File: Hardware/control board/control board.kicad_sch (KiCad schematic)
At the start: 11 parts, among them J1 Screw_Terminal_01x02, SW1 SW_Push

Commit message: footprint work
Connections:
- net solenoid 1/Sol port: now also A1.D23; no longer A1.D25
- net solenoid 2/Sol port: now also A1.D25; no longer A1.D26
- no-connect marks 0 -> 81

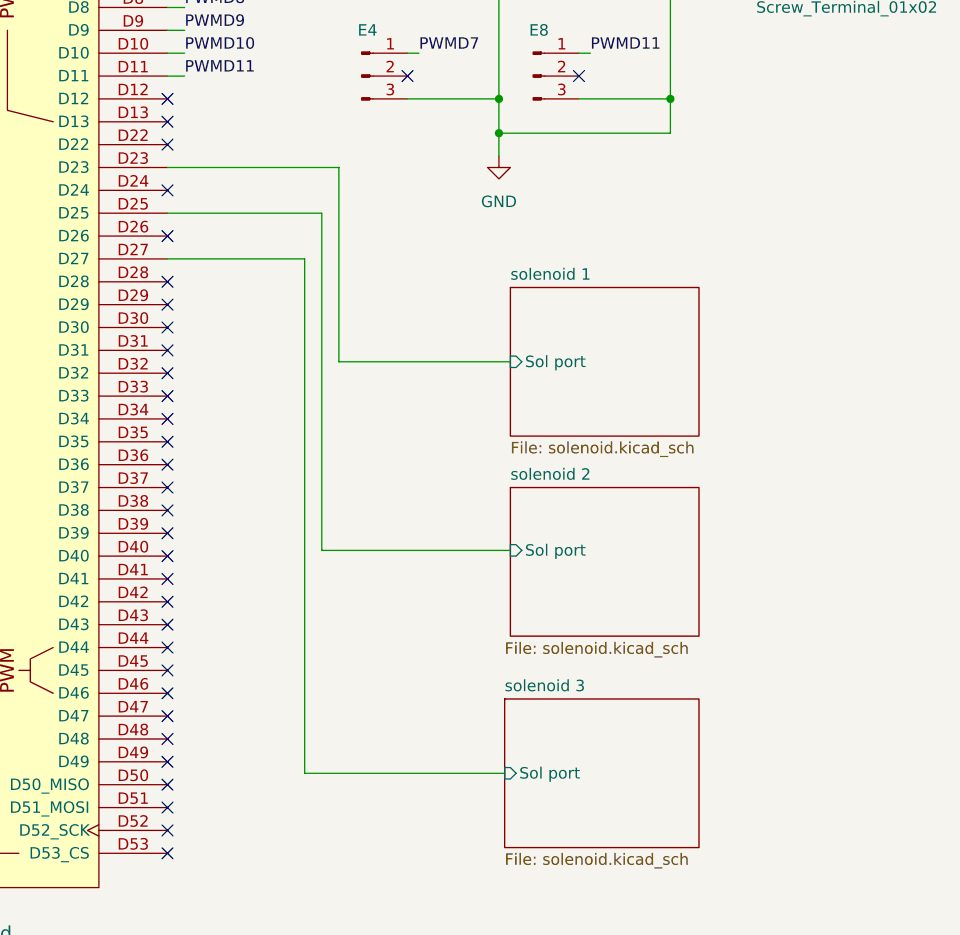
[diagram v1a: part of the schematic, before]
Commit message: laid out components prior to order
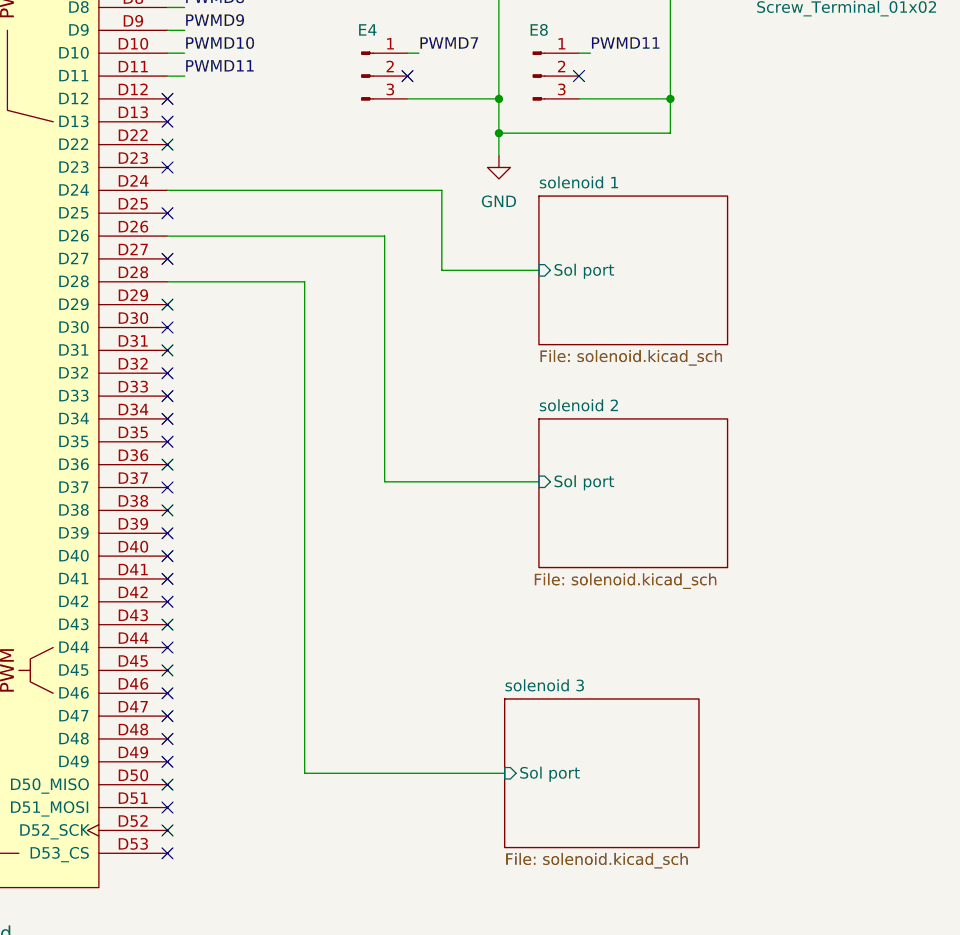
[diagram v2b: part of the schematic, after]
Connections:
- net solenoid 1/Sol port: now also A1.D24; no longer A1.D23
- net solenoid 2/Sol port: now also A1.D26; no longer A1.D25
- net solenoid 3/Sol port: now also A1.D28; no longer A1.D27
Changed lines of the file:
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@@
   (no_connect (at 93.345 129.54))
   (no_connect (at 93.345 111.76))
+  (no_connect (at 93.345 76.2))
   (no_connect (at 27.305 129.54))
   (no_connect (at 93.345 134.62))
@@
   (no_connect (at 27.305 48.26))
   (no_connect (at 27.305 40.64))
-  (no_connect (at 93.345 78.74))
   (no_connect (at 61.595 26.67))
   (no_connect (at 27.305 55.88))
@@
   (no_connect (at 93.345 96.52))
   (no_connect (at 93.345 124.46))
+  (no_connect (at 93.345 81.28))
   (no_connect (at 27.305 109.22))
   (no_connect (at 27.305 93.98))
-  (no_connect (at 93.345 83.82))
   (no_connect (at 53.975 26.67))
   (no_connect (at 27.305 134.62))
@@
   (no_connect (at 93.345 114.3))
   (no_connect (at 93.345 91.44))
+  (no_connect (at 93.345 71.12))
   (no_connect (at 27.305 96.52))
   (no_connect (at 27.305 104.14))
@@
   (no_connect (at 27.305 111.76))
   (no_connect (at 27.305 73.66))
-  (no_connect (at 93.345 73.66))
   (no_connect (at 27.305 78.74))
   (no_connect (at 93.345 139.7))
@@
   (no_connect (at 27.305 81.28))
   (no_connect (at 27.305 66.04))
+  (wire (pts (xy 134.62 82.55) (xy 123.825 82.55))
+    (stroke (width 0) (type default))
+  )
   (wire (pts (xy 139.065 50.8) (xy 149.225 50.8))
     (stroke (width 0) (type default))
   )
-  (wire (pts (xy 112.395 71.12) (xy 112.395 92.71))
-    (stroke (width 0) (type default))
-  )
   (wire (pts (xy 93.345 58.42) (xy 95.25 58.42))
     (stroke (width 0) (type default))
   )
-  (wire (pts (xy 110.49 76.2) (xy 93.345 76.2))
-    (stroke (width 0) (type default))
-  )
   (wire (pts (xy 149.225 50.8) (xy 149.225 63.5))
     (stroke (width 0) (type default))
   )
+  (wire (pts (xy 117.475 78.74) (xy 117.475 106.045))
+    (stroke (width 0) (type default))
+  )
   (wire (pts (xy 130.81 138.43) (xy 108.585 138.43))
     (stroke (width 0) (type default))
@@
     (stroke (width 0) (type default))
   )
+  (wire (pts (xy 93.345 78.74) (xy 117.475 78.74))
+    (stroke (width 0) (type default))
+  )
+  (wire (pts (xy 123.825 73.66) (xy 93.345 73.66))
+    (stroke (width 0) (type default))
+  )
   (wire (pts (xy 93.345 53.34) (xy 95.25 53.34))
     (stroke (width 0) (type default))
@@
     (stroke (width 0) (type default))
   )
-  (wire (pts (xy 131.445 113.665) (xy 110.49 113.665))
-    (stroke (width 0) (type default))
-  )
   (wire (pts (xy 23.495 137.16) (xy 23.495 139.7))
     (stroke (width 0) (type default))
@@
     (stroke (width 0) (type default))
   )
-  (wire (pts (xy 108.585 81.28) (xy 108.585 138.43))
+  (wire (pts (xy 123.825 82.55) (xy 123.825 73.66))
     (stroke (width 0) (type default))
   )
@@
     (stroke (width 0) (type default))
   )
+  (wire (pts (xy 108.585 138.43) (xy 108.585 83.82))
+    (stroke (width 0) (type default))
+  )
   (wire (pts (xy 120.015 58.42) (xy 121.285 58.42))
     (stroke (width 0) (type default))
@@
     (stroke (width 0) (type default))
   )
-  (wire (pts (xy 131.445 92.71) (xy 112.395 92.71))
-    (stroke (width 0) (type default))
-  )
   (wire (pts (xy 130.175 69.85) (xy 130.175 67.31))
     (stroke (width 0) (type default))
@@
     (stroke (width 0) (type default))
   )
-  (wire (pts (xy 112.395 71.12) (xy 93.345 71.12))
-    (stroke (width 0) (type default))
-  )
   (wire (pts (xy 139.065 58.42) (xy 140.335 58.42))
     (stroke (width 0) (type default))
@@
     (stroke (width 0) (type default))
   )
+  (wire (pts (xy 117.475 106.045) (xy 134.62 106.045))
+    (stroke (width 0) (type default))
+  )
   (wire (pts (xy 120.015 25.4) (xy 130.175 25.4))
     (stroke (width 0) (type default))
@@
     (stroke (width 0) (type default))
   )
-  (wire (pts (xy 110.49 76.2) (xy 110.49 113.665))
-    (stroke (width 0) (type default))
-  )
   (wire (pts (xy 27.305 116.84) (xy 19.05 116.84))
     (stroke (width 0) (type default))
@@
     (stroke (width 0) (type default))
   )
-  (wire (pts (xy 108.585 81.28) (xy 93.345 81.28))
+  (wire (pts (xy 108.585 83.82) (xy 93.345 83.82))
     (stroke (width 0) (type default))
   )
@@
     )
   )
-  (sheet (at 131.445 106.68) (size 20.955 16.51)
+  (sheet (at 134.62 99.06) (size 20.955 16.51)
     (stroke (width 0.1524) (type solid))
     (fill (color 0 0 0 0.0000))
-    (property "Sheetname" "solenoid 2" (at 131.445 105.9684 0)
+    (property "Sheetname" "solenoid 2" (at 134.62 98.3484 0)
       (effects (font (size 1.27 1.27)) (justify left bottom))
     )
-    (property "Sheetfile" "solenoid.kicad_sch" (at 130.81 123.825 0)
+    (property "Sheetfile" "solenoid.kicad_sch" (at 133.985 116.205 0)
       (effects (font (size 1.27 1.27)) (justify left top))
     )
-    (pin "Sol port" input (at 131.445 113.665 180)
+    (pin "Sol port" input (at 134.62 106.045 180)
       (effects (font (size 1.27 1.27)) (justify left))
     )
@@
     )
   )
-  (sheet (at 131.445 84.455) (size 20.955 16.51) (fields_autoplaced)
+  (sheet (at 134.62 74.295) (size 20.955 16.51) (fields_autoplaced)
     (stroke (width 0.1524) (type solid))
     (fill (color 0 0 0 0.0000))
-    (property "Sheetname" "solenoid 1" (at 131.445 83.7434 0)
+    (property "Sheetname" "solenoid 1" (at 134.62 73.5834 0)
       (effects (font (size 1.27 1.27)) (justify left bottom))
     )
-    (property "Sheetfile" "solenoid.kicad_sch" (at 131.445 101.5496 0)
+    (property "Sheetfile" "solenoid.kicad_sch" (at 134.62 91.3896 0)
       (effects (font (size 1.27 1.27)) (justify left top))
     )
-    (pin "Sol port" input (at 131.445 92.71 180)
+    (pin "Sol port" input (at 134.62 82.55 180)
       (effects (font (size 1.27 1.27)) (justify left))
     )

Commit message: control board clean up
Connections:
- net +14.8V: now also J1.2 (Pin_2); no longer J1.1 (Pin_1)
- net GND: now also E1.1 (Pin_1), E2.1 (Pin_1), E4.1 (Pin_1), E5.1 (Pin_1), E6.1 (Pin_1), E7.1 (Pin_1), E8.1 (Pin_1), J1.1 (Pin_1); no longer E1.3 (Pin_3), E2.3 (Pin_3), E3.3 (Pin_3), E4.3 (Pin_3), E5.3 (Pin_3), E6.3 (Pin_3), E7.3 (Pin_3), E8.3 (Pin_3), J1.2 (Pin_2)
- net PWMD10: now also E7.3 (Pin_3); no longer E7.1 (Pin_1)
- net PWMD11: now also E8.3 (Pin_3); no longer E8.1 (Pin_1)
- net PWMD4: now also E1.3 (Pin_3); no longer E1.1 (Pin_1)
- net PWMD5: now also E2.3 (Pin_3); no longer E2.1 (Pin_1)
- net PWMD6: now also E3.3 (Pin_3); no longer E3.1 (Pin_1)
- net PWMD7: now also E4.3 (Pin_3); no longer E4.1 (Pin_1)
- net PWMD8: now also E5.3 (Pin_3); no longer E5.1 (Pin_1)
- net PWMD9: now also E6.3 (Pin_3); no longer E6.1 (Pin_1)
- net solenoid 1/Sol port renamed sol 1
- net solenoid 2/Sol port renamed sol 2
- net solenoid 3/Sol port renamed sol 3
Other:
- moved on the sheet: E1, E2, E3, E4, E5, E6, E7, E8, J1

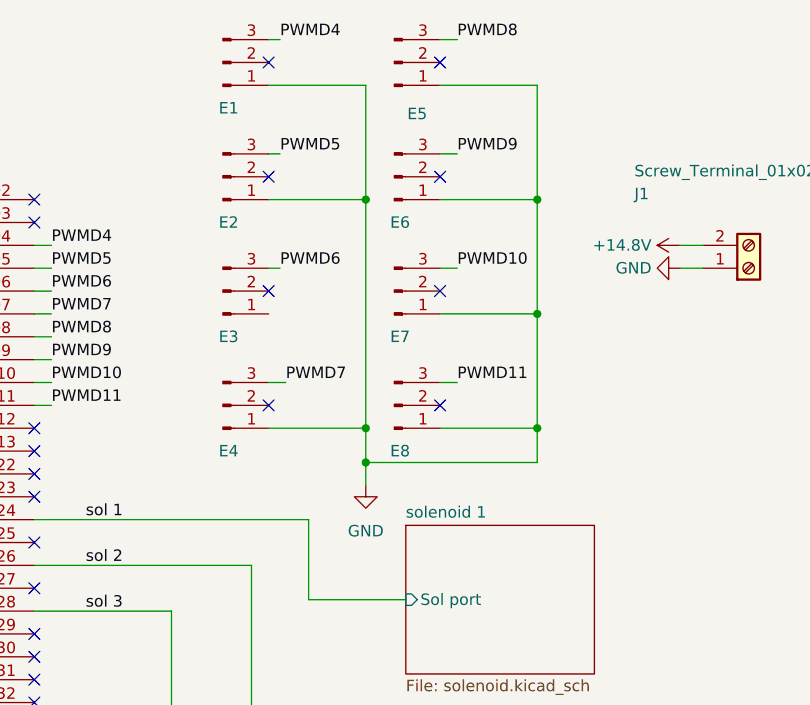
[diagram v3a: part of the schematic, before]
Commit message: fixed nmos footprint
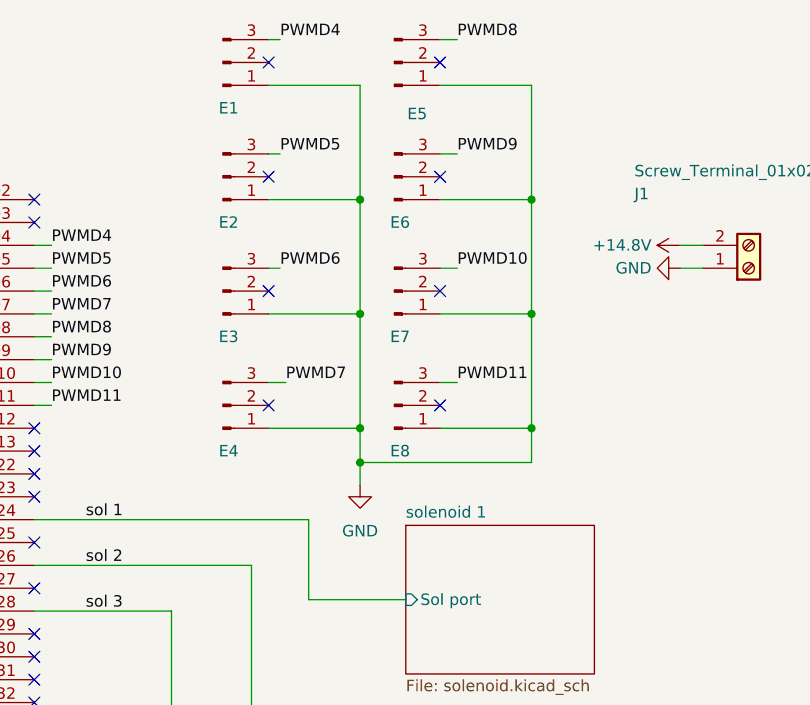
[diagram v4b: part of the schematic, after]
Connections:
- net GND: now also E3.1 (Pin_1)
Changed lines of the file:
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@@
 (kicad_sch (version 20230121) (generator eeschema)
   (paper "A4")
-  (junction (at 130.175 38.1) (diameter 0) (color 0 0 0 0)
-  )
-  (junction (at 149.225 50.8) (diameter 0) (color 0 0 0 0)
-  )
-  (junction (at 130.175 67.31) (diameter 0) (color 0 0 0 0)
+  (junction (at 129.54 38.1) (diameter 0) (color 0 0 0 0)
+  )
+  (junction (at 148.59 50.8) (diameter 0) (color 0 0 0 0)
+  )
+  (junction (at 129.54 67.31) (diameter 0) (color 0 0 0 0)
   )
   (junction (at 23.495 144.78) (diameter 0) (color 0 0 0 0)
   )
-  (junction (at 149.225 63.5) (diameter 0) (color 0 0 0 0)
-  )
-  (junction (at 130.175 63.5) (diameter 0) (color 0 0 0 0)
+  (junction (at 129.54 50.8) (diameter 0) (color 0 0 0 0)
+  )
+  (junction (at 148.59 63.5) (diameter 0) (color 0 0 0 0)
+  )
+  (junction (at 129.54 63.5) (diameter 0) (color 0 0 0 0)
   )
   (junction (at 23.495 139.7) (diameter 0) (color 0 0 0 0)
@@
   (junction (at 23.495 147.32) (diameter 0) (color 0 0 0 0)
   )
-  (junction (at 149.225 38.1) (diameter 0) (color 0 0 0 0)
+  (junction (at 148.59 38.1) (diameter 0) (color 0 0 0 0)
   )
   (no_connect (at 93.345 104.14))
@@
     (stroke (width 0) (type default))
   )
-  (wire (pts (xy 138.43 50.8) (xy 149.225 50.8))
+  (wire (pts (xy 129.54 50.8) (xy 129.54 63.5))
+    (stroke (width 0) (type default))
+  )
+  (wire (pts (xy 138.43 50.8) (xy 148.59 50.8))
     (stroke (width 0) (type default))
   )
@@
     (stroke (width 0) (type default))
   )
-  (wire (pts (xy 149.225 50.8) (xy 149.225 63.5))
+  (wire (pts (xy 148.59 50.8) (xy 148.59 63.5))
     (stroke (width 0) (type default))
   )
@@
     (stroke (width 0) (type default))
   )
-  (wire (pts (xy 149.225 38.1) (xy 149.225 50.8))
+  (wire (pts (xy 148.59 38.1) (xy 148.59 50.8))
     (stroke (width 0) (type default))
   )
@@
     (stroke (width 0) (type default))
   )
-  (wire (pts (xy 138.43 63.5) (xy 149.225 63.5))
+  (wire (pts (xy 138.43 63.5) (xy 148.59 63.5))
     (stroke (width 0) (type default))
   )
@@
     (stroke (width 0) (type default))
   )
-  (wire (pts (xy 130.175 63.5) (xy 130.175 67.31))
+  (wire (pts (xy 129.54 63.5) (xy 129.54 67.31))
     (stroke (width 0) (type default))
   )
@@
     (stroke (width 0) (type default))
   )
-  (wire (pts (xy 130.175 25.4) (xy 130.175 38.1))
+  (wire (pts (xy 129.54 25.4) (xy 129.54 38.1))
     (stroke (width 0) (type default))
   )
@@
     (stroke (width 0) (type default))
   )
-  (wire (pts (xy 119.38 38.1) (xy 130.175 38.1))
+  (wire (pts (xy 119.38 38.1) (xy 129.54 38.1))
     (stroke (width 0) (type default))
   )
@@
     (stroke (width 0) (type default))
   )
-  (wire (pts (xy 130.175 69.85) (xy 130.175 67.31))
+  (wire (pts (xy 129.54 69.85) (xy 129.54 67.31))
     (stroke (width 0) (type default))
   )
@@
     (stroke (width 0) (type default))
   )
-  (wire (pts (xy 149.225 25.4) (xy 149.225 38.1))
-    (stroke (width 0) (type default))
-  )
-  (wire (pts (xy 149.225 67.31) (xy 130.175 67.31))
+  (wire (pts (xy 148.59 25.4) (xy 148.59 38.1))
+    (stroke (width 0) (type default))
+  )
+  (wire (pts (xy 148.59 67.31) (xy 129.54 67.31))
     (stroke (width 0) (type default))
   )
@@
     (stroke (width 0) (type default))
   )
-  (wire (pts (xy 119.38 63.5) (xy 130.175 63.5))
+  (wire (pts (xy 119.38 63.5) (xy 129.54 63.5))
     (stroke (width 0) (type default))
   )
@@
     (stroke (width 0) (type default))
   )
-  (wire (pts (xy 130.175 38.1) (xy 130.175 63.5))
+  (wire (pts (xy 129.54 38.1) (xy 129.54 50.8))
     (stroke (width 0) (type default))
   )
@@
     (stroke (width 0) (type default))
   )
-  (wire (pts (xy 138.43 38.1) (xy 149.225 38.1))
+  (wire (pts (xy 138.43 38.1) (xy 148.59 38.1))
+    (stroke (width 0) (type default))
+  )
+  (wire (pts (xy 119.38 50.8) (xy 129.54 50.8))
     (stroke (width 0) (type default))
   )
@@
     (stroke (width 0) (type default))
   )
-  (wire (pts (xy 138.43 25.4) (xy 149.225 25.4))
-    (stroke (width 0) (type default))
-  )
-  (wire (pts (xy 149.225 63.5) (xy 149.225 67.31))
+  (wire (pts (xy 138.43 25.4) (xy 148.59 25.4))
+    (stroke (width 0) (type default))
+  )
+  (wire (pts (xy 148.59 63.5) (xy 148.59 67.31))
     (stroke (width 0) (type default))
   )
@@
     (stroke (width 0) (type default))
   )
-  (wire (pts (xy 119.38 25.4) (xy 130.175 25.4))
+  (wire (pts (xy 119.38 25.4) (xy 129.54 25.4))
     (stroke (width 0) (type default))
   )
@@
     )
   )
-  (symbol (lib_id "power:GND") (at 130.175 69.85 0) (unit 1)
+  (symbol (lib_id "power:GND") (at 129.54 69.85 0) (unit 1)
     (in_bom yes) (on_board yes) (dnp no) (fields_autoplaced)
-    (property "Reference" "#PWR01" (at 130.175 76.2 0)
-      (effects (font (size 1.27 1.27)) hide)
-    )
-    (property "Value" "GND" (at 130.175 74.93 0)
-      (effects (font (size 1.27 1.27)))
-    )
-    (property "Footprint" "" (at 130.175 69.85 0)
-      (effects (font (size 1.27 1.27)) hide)
-    )
-    (property "Datasheet" "" (at 130.175 69.85 0)
-      (effects (font (size 1.27 1.27)) hide)
-    )
+    (property "Reference" "#PWR01" (at 129.54 76.2 0)
+      (effects (font (size 1.27 1.27)) hide)
+    )
+    (property "Value" "GND" (at 129.54 74.93 0)
+      (effects (font (size 1.27 1.27)))
+    )
+    (property "Footprint" "" (at 129.54 69.85 0)
+      (effects (font (size 1.27 1.27)) hide)
+    )
+    (property "Datasheet" "" (at 129.54 69.85 0)
+      (effects (font (size 1.27 1.27)) hide)
+    )

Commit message: corrected pin headers and LED resistors
fixed pin headers and LED resistors
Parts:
- E1, E2, E3, E4, E5, E6, E7, E8: footprint Connector_PinHeader_2.00mm:PinHeader_1x03_P2.00mm_Vertical -> Connector_PinHeader_2.54mm:PinHeader_1x03_P2.54mm_Vertical
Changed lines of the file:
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@@
       (effects (font (size 1.27 1.27)) hide)
     )
-    (property "Footprint" "Connector_PinHeader_2.00mm:PinHeader_1x03_P2.00mm_Vertical" (at 133.35 22.86 0)
+    (property "Footprint" "Connector_PinHeader_2.54mm:PinHeader_1x03_P2.54mm_Vertical" (at 133.35 22.86 0)
       (effects (font (size 1.27 1.27)) hide)
     )
@@
       (effects (font (size 1.27 1.27)) hide)
     )
-    (property "Footprint" "Connector_PinHeader_2.00mm:PinHeader_1x03_P2.00mm_Vertical" (at 114.3 48.26 0)
+    (property "Footprint" "Connector_PinHeader_2.54mm:PinHeader_1x03_P2.54mm_Vertical" (at 114.3 48.26 0)
       (effects (font (size 1.27 1.27)) hide)
     )
@@
       (effects (font (size 1.27 1.27)) hide)
     )
-    (property "Footprint" "Connector_PinHeader_2.00mm:PinHeader_1x03_P2.00mm_Vertical" (at 114.3 60.96 0)
+    (property "Footprint" "Connector_PinHeader_2.54mm:PinHeader_1x03_P2.54mm_Vertical" (at 114.3 60.96 0)
       (effects (font (size 1.27 1.27)) hide)
     )
@@
       (effects (font (size 1.27 1.27)) hide)
     )
-    (property "Footprint" "Connector_PinHeader_2.00mm:PinHeader_1x03_P2.00mm_Vertical" (at 114.3 22.86 0)
+    (property "Footprint" "Connector_PinHeader_2.54mm:PinHeader_1x03_P2.54mm_Vertical" (at 114.3 22.86 0)
       (effects (font (size 1.27 1.27)) hide)
     )
@@
       (effects (font (size 1.27 1.27)) hide)
     )
-    (property "Footprint" "Connector_PinHeader_2.00mm:PinHeader_1x03_P2.00mm_Vertical" (at 133.35 60.96 0)
+    (property "Footprint" "Connector_PinHeader_2.54mm:PinHeader_1x03_P2.54mm_Vertical" (at 133.35 60.96 0)
       (effects (font (size 1.27 1.27)) hide)
     )
@@
       (effects (font (size 1.27 1.27)) hide)
     )
-    (property "Footprint" "Connector_PinHeader_2.00mm:PinHeader_1x03_P2.00mm_Vertical" (at 133.35 35.56 0)
+    (property "Footprint" "Connector_PinHeader_2.54mm:PinHeader_1x03_P2.54mm_Vertical" (at 133.35 35.56 0)
       (effects (font (size 1.27 1.27)) hide)
     )
@@
       (effects (font (size 1.27 1.27)) hide)
     )
-    (property "Footprint" "Connector_PinHeader_2.00mm:PinHeader_1x03_P2.00mm_Vertical" (at 114.3 35.56 0)
+    (property "Footprint" "Connector_PinHeader_2.54mm:PinHeader_1x03_P2.54mm_Vertical" (at 114.3 35.56 0)
       (effects (font (size 1.27 1.27)) hide)
     )
@@
       (effects (font (size 1.27 1.27)) hide)
     )
-    (property "Footprint" "Connector_PinHeader_2.00mm:PinHeader_1x03_P2.00mm_Vertical" (at 133.35 48.26 0)
-      (effects (font (size 1.27 1.27)) hide)
-    )
+    (property "Footprint" "Connector_PinHeader_2.54mm:PinHeader_1x03_P2.54mm_Vertical" (at 133.35 48.26 0)
+      (effects (font (size 1.27 1.27)) hide)
+    )
